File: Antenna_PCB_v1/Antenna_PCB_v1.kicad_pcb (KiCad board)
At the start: 2 copper layers, 50 x 20 mm, 6 parts, among them J1 Conn_Coaxial_Power, J2 Conn_Coaxial_Power

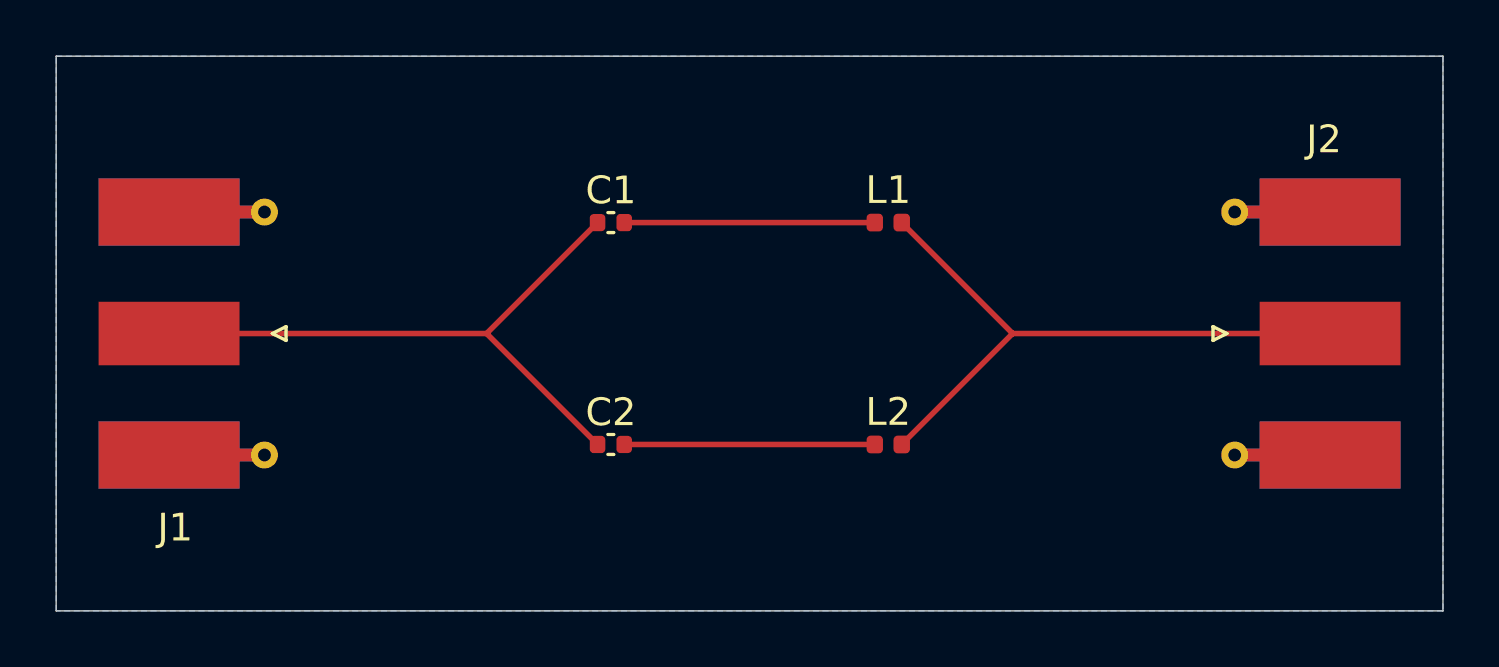
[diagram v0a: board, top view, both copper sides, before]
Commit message: Add holes to PCB
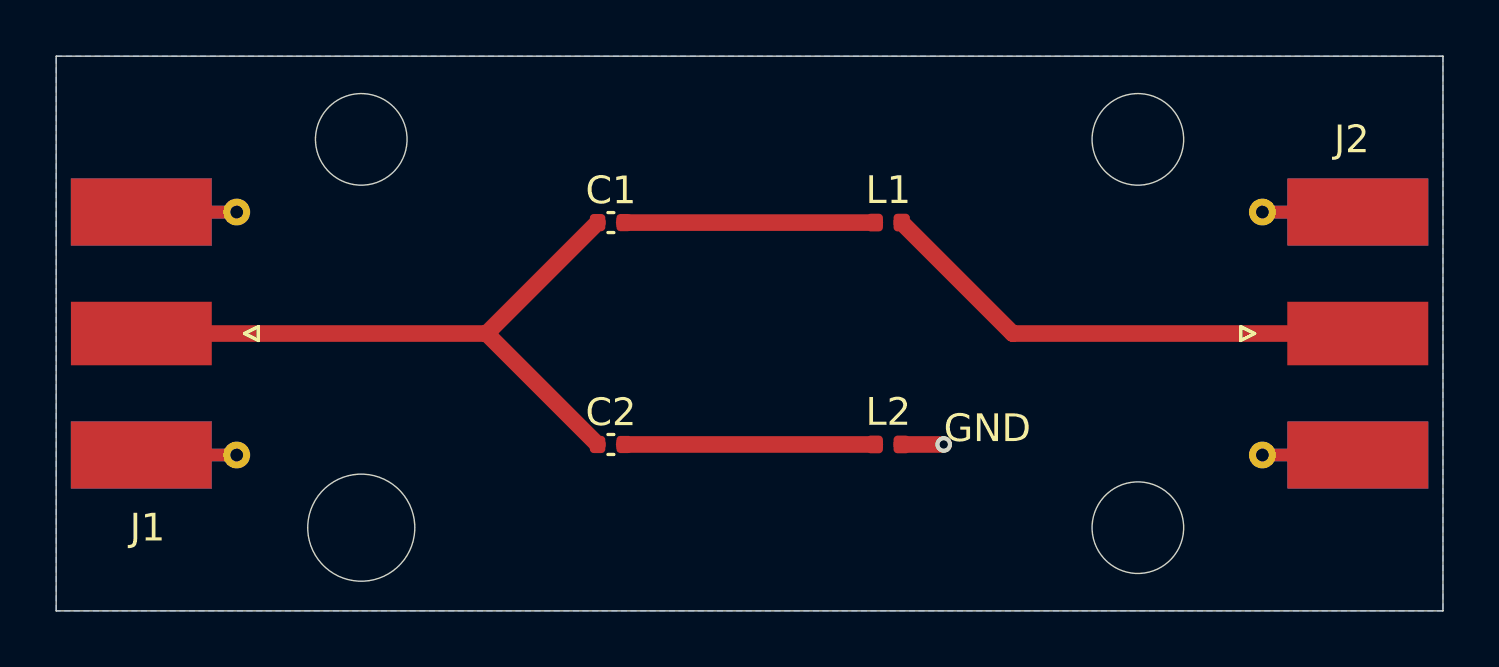
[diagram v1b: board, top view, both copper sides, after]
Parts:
- moved J1 1.00 mm to (104.8, 100.0)
- moved J2 1.00 mm to (145.2, 100.0)
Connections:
- L2 pad 2: Net-(J2-In) -> GNDREF
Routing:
- net Net-(J2-In): track 22.8 -> 18.1 mm
- net GNDREF: track 0.00 -> 1.51 mm, vias 0 -> 1
- net Net-(J1-In): track 22.8 -> 23.8 mm
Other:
- outline, holes or cut-outs redrawn
- board text added: "GND"

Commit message: Fix antenna PCB circuit
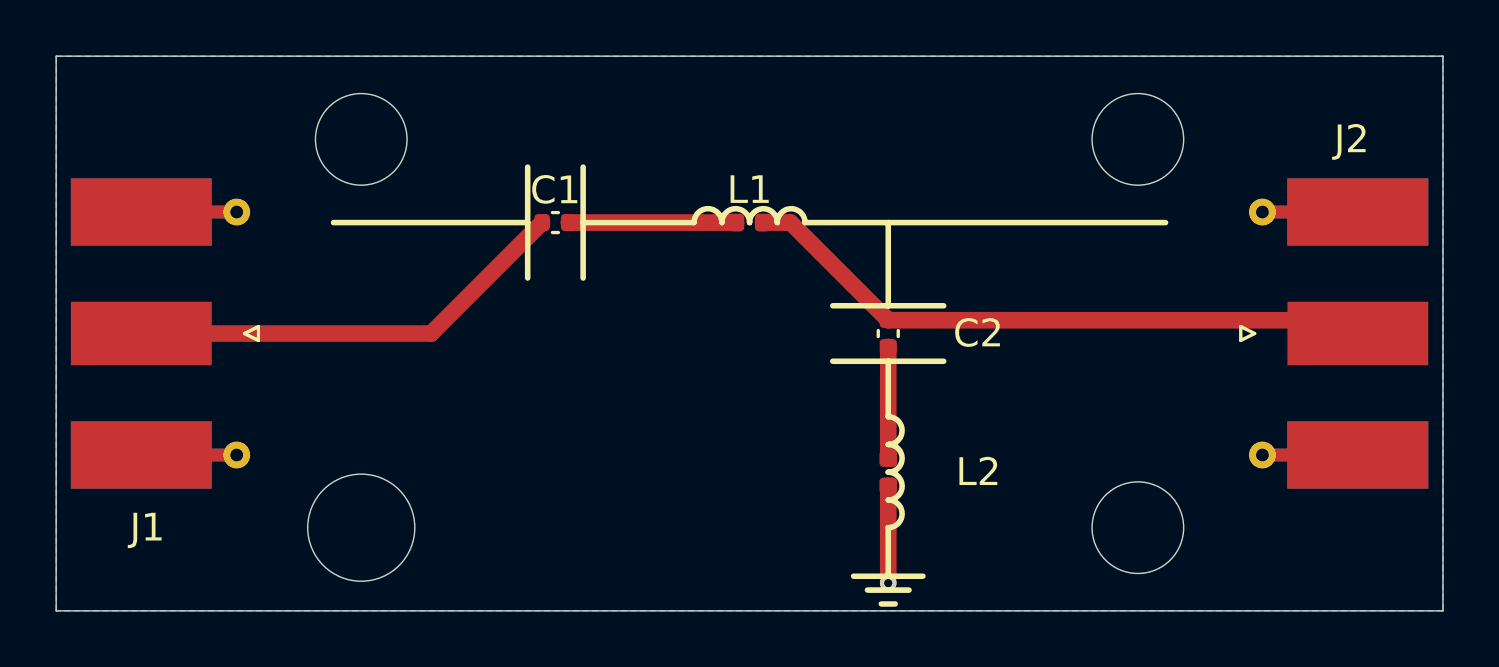
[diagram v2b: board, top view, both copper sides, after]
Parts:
- moved C2 10.8 mm to (130.0, 100.0), turned to -90 degrees
- moved L1 5.00 mm to (125.0, 96.0)
- moved C1 2.00 mm to (118.0, 96.0)
- moved L2 1.00 mm to (130.0, 105.0), turned to -90 degrees
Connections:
- C2 pad 1: Net-(J1-In) -> Net-(J2-In)
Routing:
- net Net-(J1-In): track 23.8 -> 16.1 mm
- net Net-(J2-In): track 18.1 -> 23.1 mm
- net Net-(C2-Pad2): track 9.03 -> 4.03 mm
- net Net-(C1-Pad2): track 9.03 -> 6.03 mm
- net GNDREF: track 1.51 -> 3.52 mm
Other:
- board text removed: "GND"
